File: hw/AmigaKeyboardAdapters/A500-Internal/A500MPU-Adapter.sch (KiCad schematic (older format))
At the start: 13 parts, among them P1 CONN_01X08, P2 CONN_01X08, P3 CONN_02X03, P4 CONN_01X02, P5 CONN_01X02

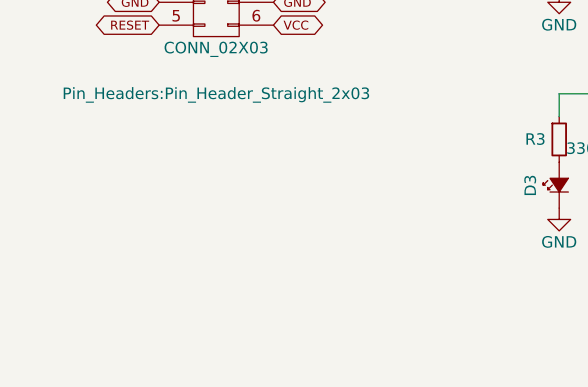
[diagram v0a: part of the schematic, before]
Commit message: Added new capacitors filter on the Vcc line (backside)
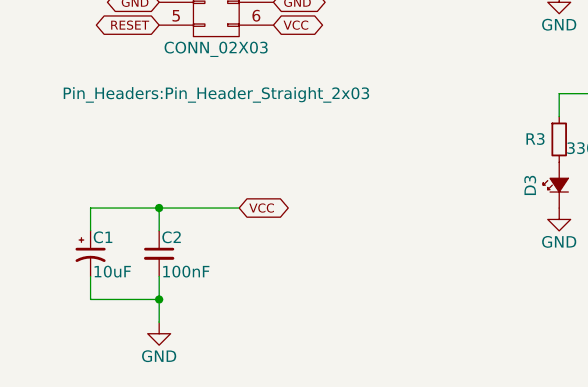
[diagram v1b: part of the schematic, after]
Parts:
- added C1: 10uF, SMD_Packages:SMD-1206_Pol, symbol CP1_Small
- added C2: 100nF, Capacitors_SMD:C_1206_HandSoldering, symbol C_Small
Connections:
- net GND: now also C1.2, C2.2
- net VCC: now also C1.1, C2.1
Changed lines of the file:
@@
 LIBS:valves
 LIBS:AmigaComponents
+LIBS:A500MPU-Adapter-cache
 EELAYER 25 0
 EELAYER END
@@
 Wire Wire Line
 	5900 3850 5900 3950
+Text GLabel 4500 4350 2    39   BiDi ~ 0
+VCC
+$Comp
+L GND #PWR014
+U 1 1 5C1ED552
+P 4150 4850
+F 0 "#PWR014" H 4150 4600 50  0001 C CNN
+F 1 "GND" H 4150 4700 50  0000 C CNN
+F 2 "" H 4150 4850 50  0001 C CNN
+F 3 "" H 4150 4850 50  0001 C CNN
+	1    4150 4850
+	1    0    0    -1
+$EndComp
+Wire Wire Line
+	3850 4350 4500 4350
+Wire Wire Line
+	4150 4350 4150 4450
+$Comp
+L C_Small C2
+U 1 1 5C1ED589
+P 4150 4550
+F 0 "C2" H 4160 4620 50  0000 L CNN
+F 1 "100nF" H 4160 4470 50  0000 L CNN
+F 2 "Capacitors_SMD:C_1206_HandSoldering" H 4150 4550 50  0001 C CNN
+F 3 "" H 4150 4550 50  0000 C CNN
+	1    4150 4550
+	1    0    0    -1
+$EndComp
+$Comp
+L CP1_Small C1
+U 1 1 5C1ED5CC
+P 3850 4550
+F 0 "C1" H 3860 4620 50  0000 L CNN
+F 1 "10uF" H 3860 4470 50  0000 L CNN
+F 2 "SMD_Packages:SMD-1206_Pol" H 3850 4550 50  0001 C CNN
+F 3 "" H 3850 4550 50  0000 C CNN
+	1    3850 4550
+	1    0    0    -1
+$EndComp
+Wire Wire Line
+	3850 4350 3850 4450
+Connection ~ 4150 4350
+Wire Wire Line
+	4150 4650 4150 4850
+Wire Wire Line
+	4150 4750 3850 4750
+Wire Wire Line
+	3850 4750 3850 4650
+Connection ~ 4150 4750
 $EndSCHEMATC
